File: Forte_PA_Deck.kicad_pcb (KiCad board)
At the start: 2 copper layers, 256 x 121 mm, 170 parts, among them J1 SMA, J2 5.08mm, J3 Keystone M5, J4 Keystone M5, J5 Conn_01x05, J6 Conn_Coaxial, Q1 MRF300AN, Q2 MRF300BN, Q3 BC846, Q4 BC846, Q5 PMOS, T1 Transformer_1P_1S, U1 AMS1117-5.0, U4 OP07, U5 LM723_DIP14

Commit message: Add files via upload
Fixed DRC shorted nets error
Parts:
- removed the R6 at (66.5, 96.1)
- added R5: 33, Resistor_SMD:R_2512_6332Metric, F.Cu at (66.5, 96.0)
- Q5: value PMOS -> AO3400A
- R20: renamed from R27; footprint Resistor_SMD:R_0603_1608Metric_Pad0.98x0.95mm_HandSolder -> Resistor_SMD:R_1206_3216Metric_Pad1.30x1.75mm_HandSolder
- moved R29 4.53 mm to (45.0, 55.3), turned to -90 degrees
- moved R20 2.29 mm to (78.7, 43.6)
- moved R31 1.83 mm to (49.5, 52.0), turned to 0 degrees
- moved Q4 0.95 mm to (48.0, 63.1)
- moved R27 0.95 mm to (44.2, 58.5)
- moved R28 0.95 mm to (44.2, 62.1)
- moved Q3 0.90 mm to (48.0, 59.4)
- moved C5 0.62 mm to (76.2, 92.8)
- moved R8 0.60 mm to (81.5, 92.8)
- moved Q5 0.45 mm to (47.7, 55.0), turned to -90 degrees
- moved C45 0.40 mm to (75.4, 42.4)
- moved R34 0.35 mm to (59.5, 61.5)
- moved C6 0.10 mm to (76.2, 99.7)
- renumbered C19 to C10, C14 to C11, C15 to C12, C5 to C13, C20 to C14, C6 to C15, C21 to C16, C9 to C17, C32 to C18, C12 to C19, C33 to C20, C13 to C21, C34 to C22, C16 to C23, C35 to C24, C17 to C25, C22 to C26, C23 to C27, C24 to C28, C25 to C29, C7 to C3, C26 to C30, C27 to C31, C28 to C32, C29 to C33, C30 to C34, C31 to C35, C8 to C4, C41 to C40, C43 to C41, C44 to C42, C40 to C43, C42 to C44, C49 to C45, C50 to C46, C201 to C47, C204 to C48, C202 to C49, C10 to C5, C205 to C50, C203 to C51, C206 to C52, C51 to C53, C52 to C54, C53 to C55, C54 to C56, C55 to C57, C56 to C58, C57 to C59, C11 to C6, C58 to C60, C59 to C61, C60 to C62, C61 to C63, C62 to C64, C63 to C65, C64 to C66, C65 to C67, C66 to C68, C67 to C69, C3 to C7, C68 to C70, C69 to C71, C70 to C72, C71 to C73, C18 to C8, C4 to C9, D11 to D10, D10 to D11, D201 to D16, D202 to D17, D16 to D18, L3 to L2, L6 to L4, L7 to L5, L8 to L6, L201 to L7, L202 to L8, R20 to R21, R21 to R22, R28 to R23, R22 to R24, R201 to R25, R202 to R26, R29 to R27, R30 to R28, R31 to R29, R32 to R30, R33 to R31, R34 to R32, R35 to R33, R36 to R34, R37 to R35, R38 to R36, R39 to R37, R40 to R38, R41 to R39, R5 to R4, R42 to R40, R43 to R41, R44 to R42, R45 to R43, R46 to R44, R47 to R45, R48 to R46, R49 to R47, R50 to R48, R4 to R6, RV3 to RV1, RV4 to RV2, RV5 to RV3, RV6 to RV4, RV7 to RV5, U4 to U2, U5 to U3
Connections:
- Q5 pad 2: +12V -> Net-(Q5-S)
- Q5 pad 3: Net-(Q5-D) -> +12V
- R31 pad 1: Net-(Q5-D) -> Net-(Q5-S)
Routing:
- net Net-(D14-K): track 146.6 -> 167.0 mm
- net Net-(D3-K): track 15.8 -> 0.00 mm
- net /To_GateB: track 0.00 -> 15.8 mm
- net Net-(D2-A): track 15.8 -> 0.00 mm
- net /To_GateA: track 0.00 -> 15.8 mm
- net Net-(Q5-S): track 0.00 -> 3.34 mm
- net Net-(U2--): track 7.20 -> 9.83 mm
- net Net-(Q3-C): track 7.64 -> 10.1 mm
- net /Bias_regulation/Bias_DC_IN: track 29.6 -> 31.7 mm
- net Net-(L8-Pad2): track 0.00 -> 2.00 mm
- net Net-(L7-Pad2): track 0.00 -> 2.00 mm
- net +12V: track 15.8 -> 14.0 mm
- net /Bias_regulation/Bias_EN: track 21.2 -> 20.6 mm
- net GND: vias 1041 -> 1057

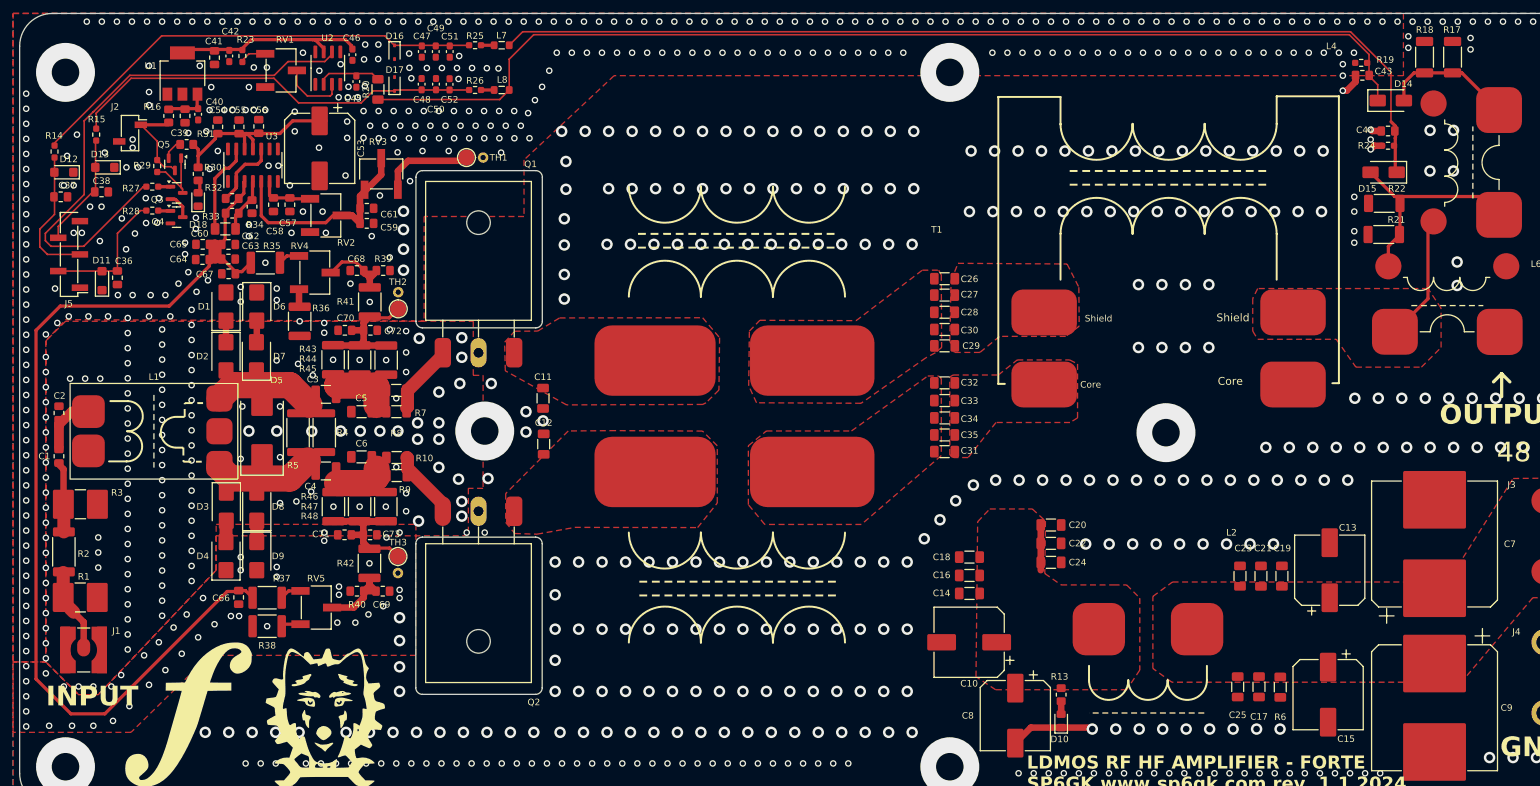
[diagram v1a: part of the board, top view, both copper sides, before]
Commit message: Ready to Order
Applied minor changes in preparation to order CPBs and components.
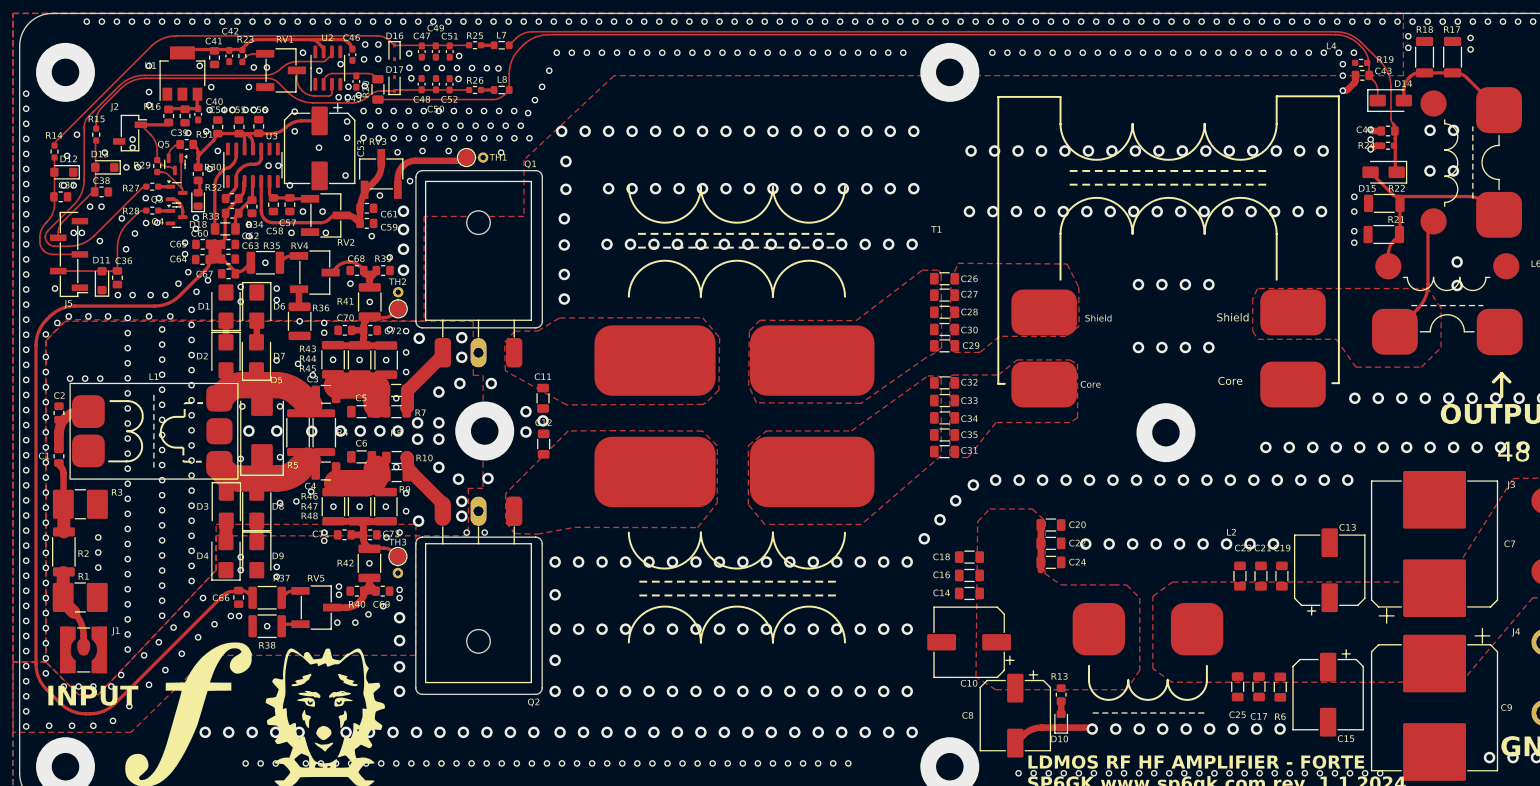
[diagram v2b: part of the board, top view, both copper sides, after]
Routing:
- net /Bias_regulation/Bias_Voltage: track 146.9 -> 144.9 mm
- net /Bias_regulation/~{HIGH_SWR}: track 82.7 -> 81.2 mm
- net Net-(D14-K): track 167.0 -> 165.8 mm
- net Net-(J1-In): track 14.7 -> 13.6 mm
- net /SWR_Meter/REF_PWR: track 63.9 -> 62.8 mm
- net Net-(D15-K): track 153.7 -> 152.9 mm
- net Net-(U3-+): track 31.8 -> 31.0 mm
- net Net-(D12-A2): track 21.2 -> 20.6 mm
